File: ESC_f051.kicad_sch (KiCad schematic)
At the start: 56 parts, among them Q1 2N7002, Q2 2N7002, Q3 2N7002, Q4 AO4407A, Q5 AO4406A, Q6 AO4407A, Q7 AO4406A, Q8 AO4407A, Q9 AO4406A, U1 XC6206PxxxMR, U2 STM32F051K8Tx

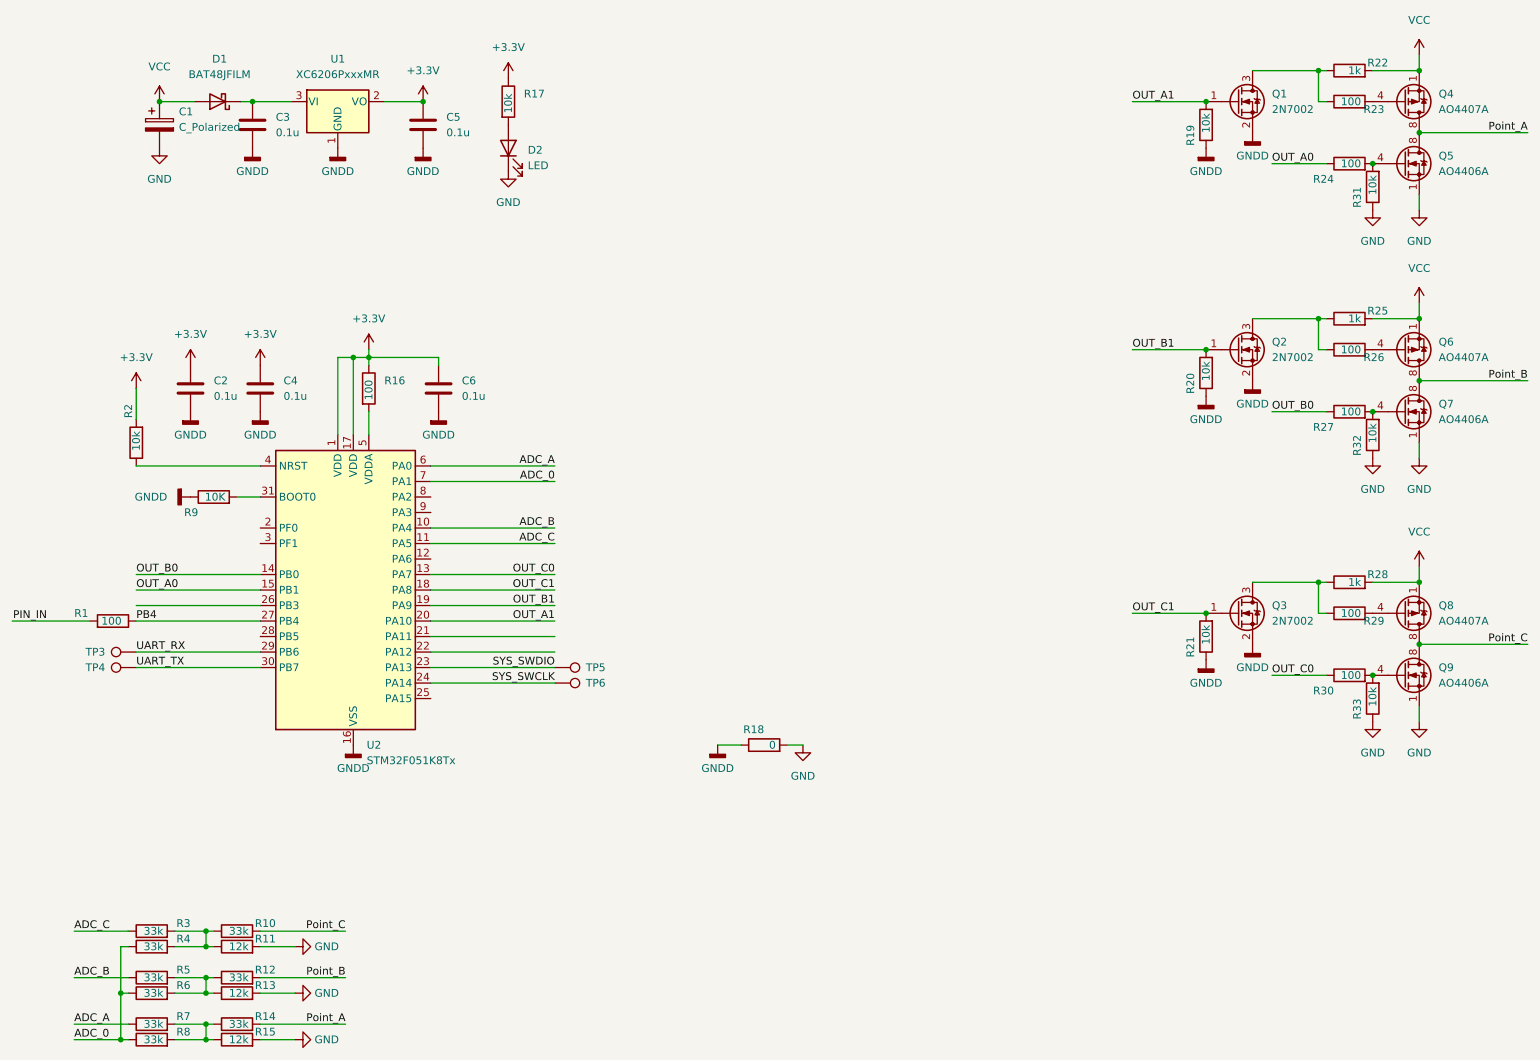
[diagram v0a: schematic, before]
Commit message: reduced the size
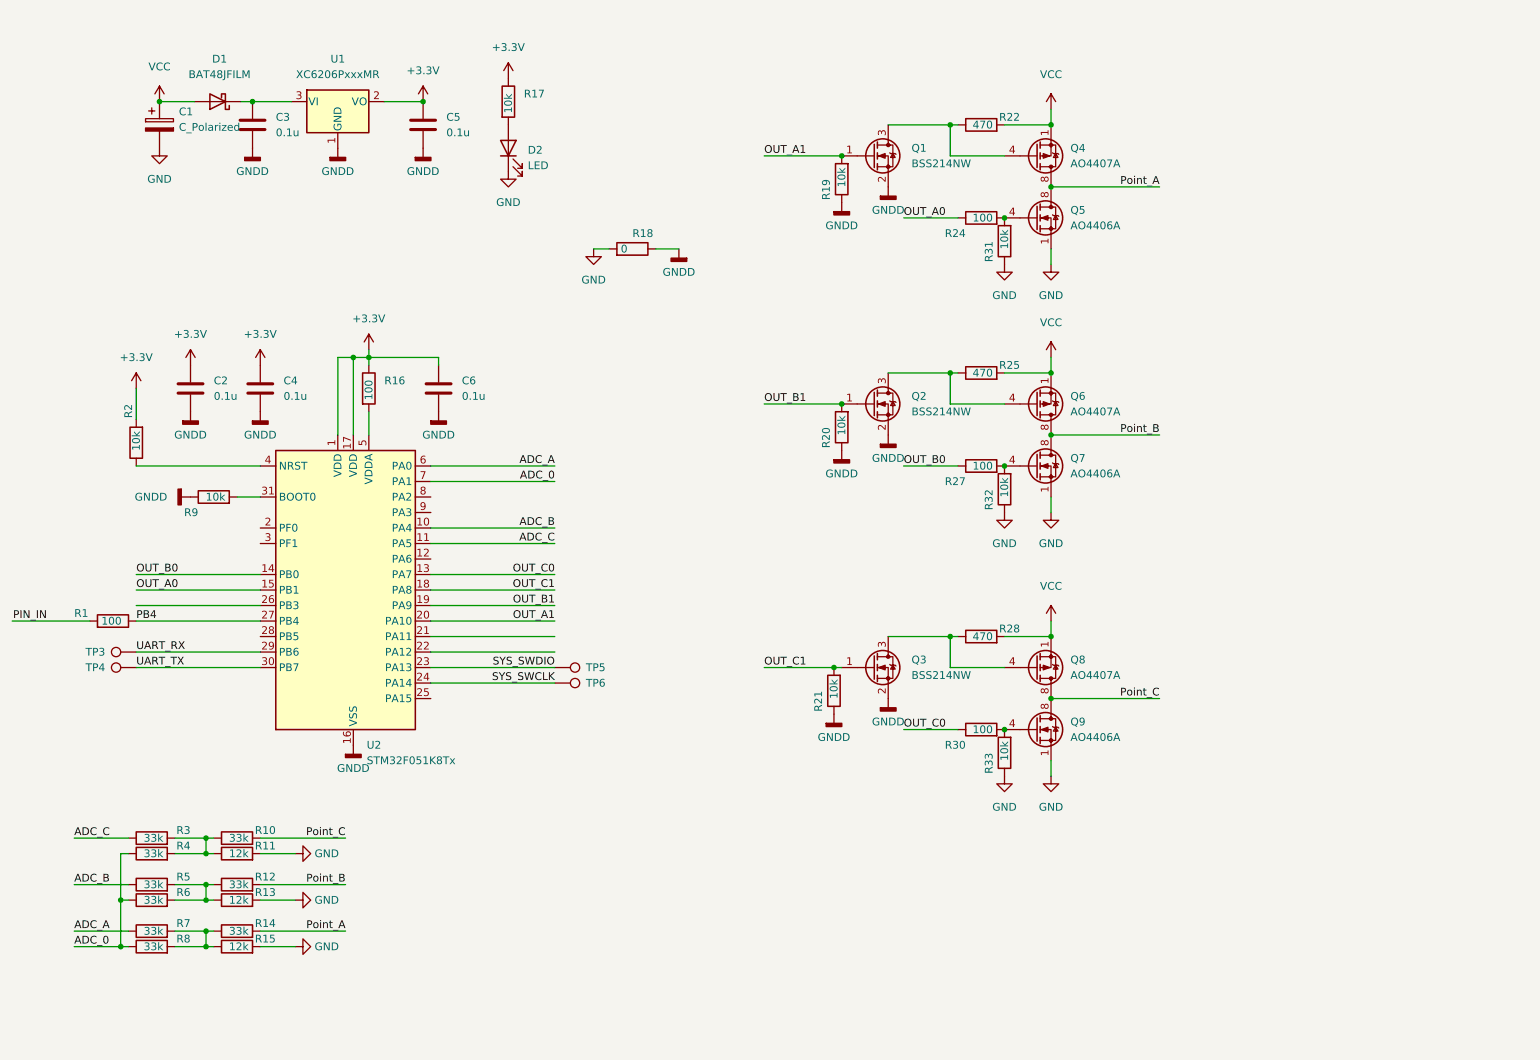
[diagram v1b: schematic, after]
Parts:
- removed Q1, Q2, Q3: 2N7002, Package_TO_SOT_SMD:SOT-23, symbol Transistor_FET:2N7002
- removed R23, R26, R29: 100, Resistor_SMD:R_0603_1608Metric, symbol Device:R
- added Q1, Q2, Q3: BSS214NW, Package_TO_SOT_SMD:SOT-323_SC-70, symbol Transistor_FET:BSS214NW
- C2, C3, C4, C5, C6: footprint Capacitor_SMD:C_0603_1608Metric -> Capacitor_SMD:C_0402_1005Metric
- R1, R10, R11, R12, R13, R14, R15, R16, R17, R18, R19, R2, R20, R21, R24, R27, R3, R30, R31, R32, R33, R4, R5, R6, R7, R8: footprint Resistor_SMD:R_0603_1608Metric -> Resistor_SMD:R_0402_1005Metric
- R22, R25, R28: value 1k -> 470; footprint Resistor_SMD:R_0603_1608Metric -> Resistor_SMD:R_0402_1005Metric
- R9: value 10K -> 10k; footprint Resistor_SMD:R_0603_1608Metric -> Resistor_SMD:R_0402_1005Metric
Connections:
- net GNDD: now also Q1.2 (S), Q2.2 (S), Q3.2 (S)
- net OUT_A1: now also Q1.1 (G)
- net OUT_B1: now also Q2.1 (G)
- net OUT_C1: now also Q3.1 (G)
- net at R25.1: now also Q6.4 (G), Q2.3 (D)
- net at R22.1: now also Q4.4 (G), Q1.3 (D)
- net at Q8.4 (G): now also R28.1, Q3.3 (D)
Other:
- moved on the sheet: Q4, Q5, Q6, Q7, Q8, Q9, R10, R11, R12, R13, R14, R15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
